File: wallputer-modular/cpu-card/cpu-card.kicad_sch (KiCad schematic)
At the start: 1 part

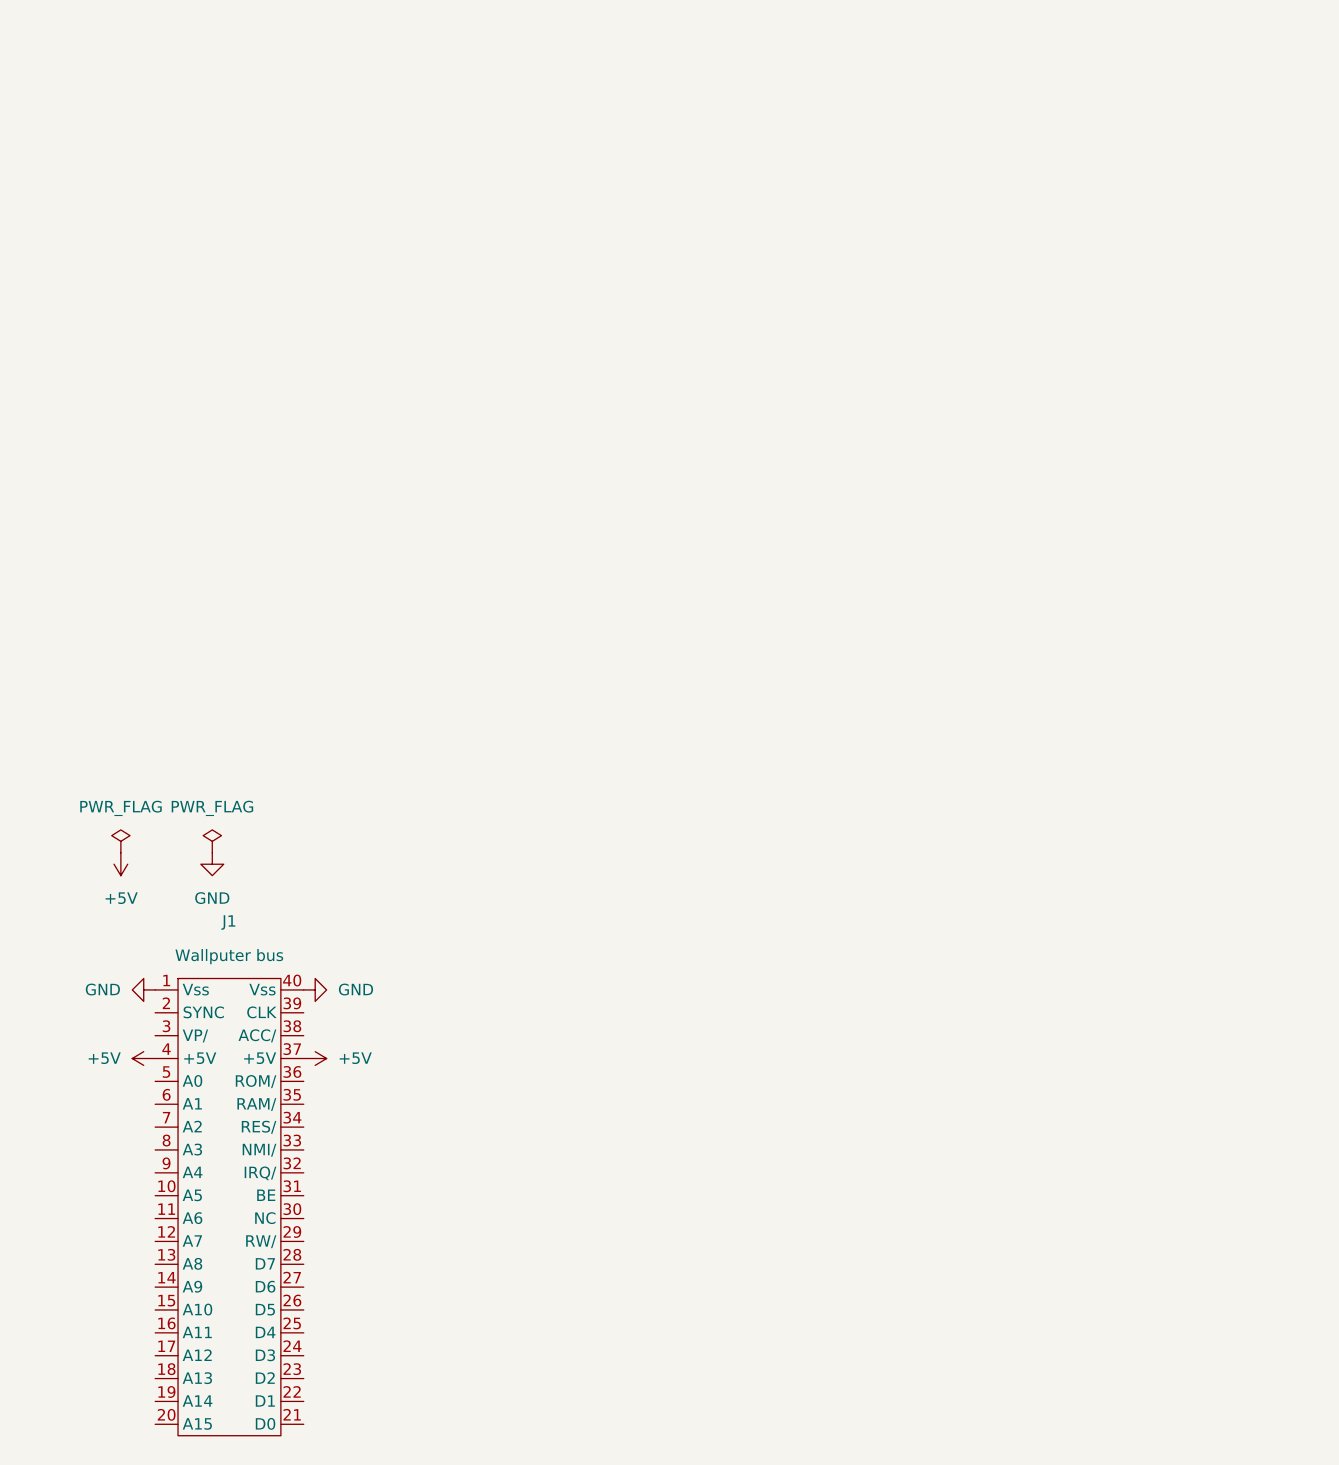
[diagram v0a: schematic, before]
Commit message: start on cpu card
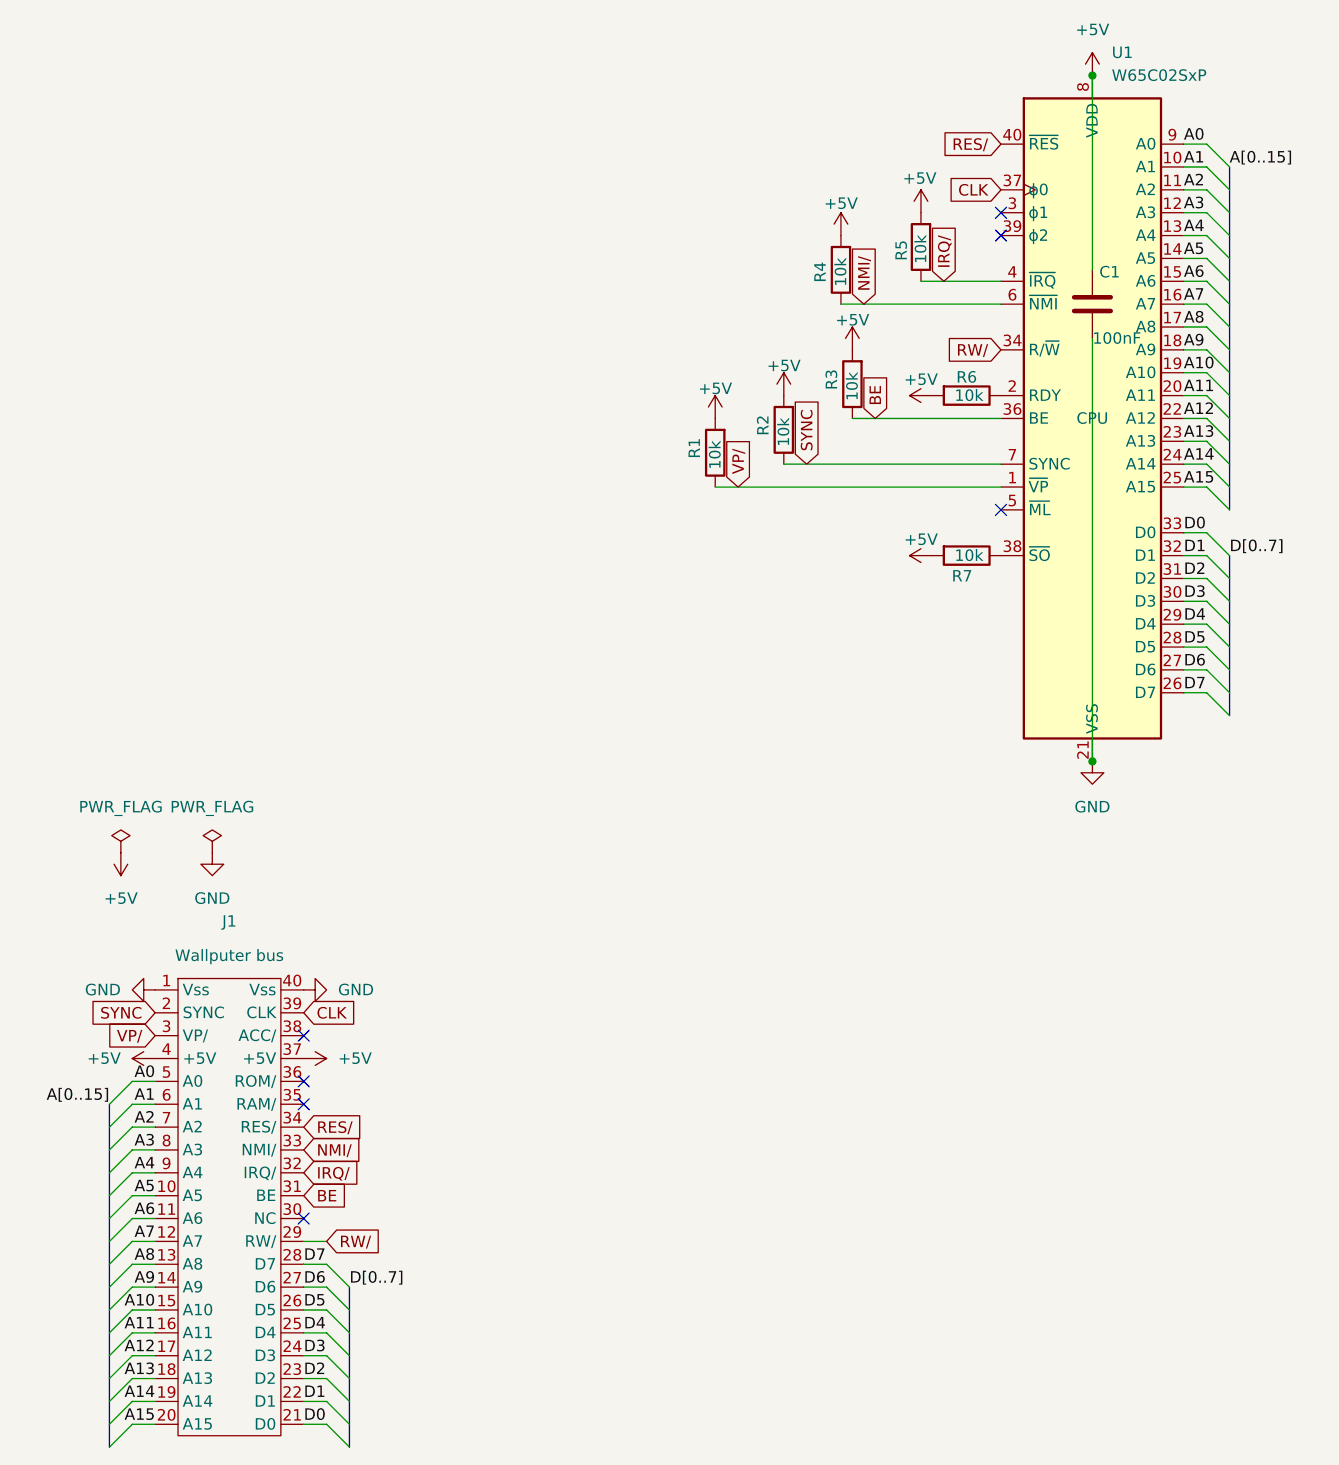
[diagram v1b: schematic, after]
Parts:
- added C1: 100nF, Capacitor_THT:C_Disc_D5.0mm_W2.5mm_P5.00mm, symbol Device:C
- added R1, R2, R3, R4, R5, R6, R7: 10k, Resistor_THT:R_Axial_DIN0204_L3.6mm_D1.6mm_P2.54mm_Vertical, symbol Device:R
- added U1: W65C02SxP, Package_DIP:DIP-40_W15.24mm_Socket, symbol 65xx-library:W65C02SxP
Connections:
- net +5V: now also C1.1, R1.2, R2.2, R3.2, R4.2, R5.2, R6.2, R7.2, U1.8 (VDD)
- net GND: now also C1.2, U1.21 (VSS)
- net A5: now reaches J1.10 (A5)
- net A5: now also U1.14 (A5)
- net A6: now reaches J1.11 (A6)
- net A6: now also U1.15 (A6)
- net A7: now reaches J1.12 (A7)
- net A7: now also U1.16 (A7)
- net A8: now reaches J1.13 (A8)
- net A8: now also U1.17 (A8)
- net A9: now reaches J1.14 (A9)
- net A9: now also U1.18 (A9)
- net A10: now reaches J1.15 (A10)
- net A10: now also U1.19 (A10)
- net A11: now reaches J1.16 (A11)
- net A11: now also U1.20 (A11)
- net A12: now reaches J1.17 (A12)
- net A12: now also U1.22 (A12)
- net A13: now reaches J1.18 (A13)
- net A13: now also U1.23 (A13)
- net A14: now reaches J1.19 (A14)
- net A14: now also U1.24 (A14)
- net SYNC: now reaches J1.2 (SYNC)
- net SYNC: now also R2.1, U1.7 (SYNC)
- net A15: now reaches J1.20 (A15)
- net A15: now also U1.25 (A15)
- net D0: now reaches J1.21 (D0)
- net D0: now also U1.33 (D0)
- net D1: now reaches J1.22 (D1)
- net D1: now also U1.32 (D1)
- net D2: now reaches J1.23 (D2)
- net D2: now also U1.31 (D2)
- net D3: now reaches J1.24 (D3)
- net D3: now also U1.30 (D3)
- net D4: now reaches J1.25 (D4)
- net D4: now also U1.29 (D4)
- net D5: now reaches J1.26 (D5)
- net D5: now also U1.28 (D5)
- net D6: now reaches J1.27 (D6)
- net D6: now also U1.27 (D6)
- net D7: now reaches J1.28 (D7)
- net D7: now also U1.26 (D7)
- net RW/: now reaches J1.29 (RW/)
- net RW/: now also U1.34 (R/~{W})
- net VP/: now reaches J1.3 (VP/)
- net VP/: now also R1.1, U1.1 (~{VP})
- net BE: now reaches J1.31 (BE)
- net BE: now also R3.1, U1.36 (BE)
- net IRQ/: now reaches J1.32 (IRQ/)
- net IRQ/: now also R5.1, U1.4 (~{IRQ})
- net NMI/: now reaches J1.33 (NMI/)
- net NMI/: now also R4.1, U1.6 (~{NMI})
- net RES/: now reaches J1.34 (RES/)
- net RES/: now also U1.40 (~{RES})
- net CLK: now reaches J1.39 (CLK)
- net CLK: now also U1.37 (ϕ0)
- net A0: now reaches J1.5 (A0)
- net A0: now also U1.9 (A0)
- net A1: now reaches J1.6 (A1)
- net A1: now also U1.10 (A1)
- net A2: now reaches J1.7 (A2)
- net A2: now also U1.11 (A2)
- net A3: now reaches J1.8 (A3)
- net A3: now also U1.12 (A3)
- net A4: now reaches J1.9 (A4)
- net A4: now also U1.13 (A4)
- new net: R7.1, U1.38 (~{SO})
- new net: R6.1, U1.2 (RDY)
- no-connect marks 0 -> 7

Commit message: do cpu card layout; add git hook; fix project settings
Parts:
- removed R1, R2: 10k, Resistor_THT:R_Axial_DIN0204_L3.6mm_D1.6mm_P2.54mm_Vertical, symbol Device:R
- added C2: 100nF, Capacitor_THT:C_Disc_D5.0mm_W2.5mm_P5.00mm, symbol Device:C
- added R8: 10k, Resistor_THT:R_Axial_DIN0204_L3.6mm_D1.6mm_P2.54mm_Vertical, symbol Device:R
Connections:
- net +5V: now also C2.2, R8.2
- net GND: now also C2.1
- net RES/: now also R8.1
